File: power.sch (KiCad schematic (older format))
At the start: 25 parts, among them P24 CONN_2, Q1 MOS_P, Q2 MOS_N, Q3 MOS_P, SW3 SPST, SW4 SPST, U8 MCP73832, U9 MCP1700

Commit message: WT12 breakout headers are now in place
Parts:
- C17, C18, C19, C20: footprint (none) -> Capacitors_SMD:C_0805_HandSoldering
- JP3: footprint (none) -> replacement_kinesis_controller:JUMPER_3
- R11, R12, R13, R14, R15, R16, R17, R18, R19: footprint (none) -> Resistors_SMD:R_0805_HandSoldering
- SW3, SW4: footprint (none) -> replacement_kinesis_controller:Pin_Header_Staggered_Straight_1x02
- U9: footprint (none) -> Housings_SOT-23_SOT-143_TSOT-6:SOT23_Transistor_Handsoldering_RevB_14Mar2014
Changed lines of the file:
@@
 F 0 "C17" H 1100 1650 40  0000 L CNN
 F 1 "4.7uF" H 1100 1450 40  0000 L CNN
-F 2 "" H 1150 1400 30  0000 C CNN
+F 2 "Capacitors_SMD:C_0805_HandSoldering" H 1150 1400 30  0001 C CNN
 F 3 "" H 1050 1550 300 0000 C CNN
 	1    1050 1550
@@
 F 0 "D16" H 1500 1650 50  0000 C CNN
 F 1 "LED" H 1500 1450 50  0000 C CNN
-F 2 "" H 1500 1550 60  0000 C CNN
+F 2 "" H 1500 1550 60  0001 C CNN
 F 3 "" H 1500 1550 60  0000 C CNN
 	1    1500 1550
@@
 F 0 "U8" H 2900 1700 60  0000 C CNN
 F 1 "MCP73832" H 2900 1200 60  0000 C CNN
-F 2 "" H 2900 1500 60  0000 C CNN
+F 2 "" H 2900 1500 60  0001 C CNN
 F 3 "" H 2900 1500 60  0000 C CNN
 	1    2900 1500
@@
 F 0 "JP3" H 4200 1800 40  0000 L CNN
 F 1 "JUMPER3" H 4150 2000 40  0000 C CNN
-F 2 "" H 4150 1900 60  0000 C CNN
+F 2 "replacement_kinesis_controller:JUMPER_3" H 4150 1900 60  0001 C CNN
 F 3 "" H 4150 1900 60  0000 C CNN
 	1    4150 1900
@@
 F 0 "R18" V 3930 2200 40  0000 C CNN
 F 1 "2k" V 3857 2201 40  0000 C CNN
-F 2 "" V 3780 2200 30  0000 C CNN
+F 2 "Resistors_SMD:R_0805_HandSoldering" V 3780 2200 30  0001 C CNN
 F 3 "" H 3850 2200 30  0000 C CNN
 	1    3850 2200
@@
 F 0 "R19" V 4530 2200 40  0000 C CNN
 F 1 "10k" V 4457 2201 40  0000 C CNN
-F 2 "" V 4380 2200 30  0000 C CNN
+F 2 "Resistors_SMD:R_0805_HandSoldering" V 4380 2200 30  0001 C CNN
 F 3 "" H 4450 2200 30  0000 C CNN
 	1    4450 2200
@@
 F 0 "R20" V 4730 2200 40  0000 C CNN
 F 1 "EXTERNAL" V 4657 2201 40  0000 C CNN
-F 2 "" V 4580 2200 30  0000 C CNN
+F 2 "" V 4580 2200 30  0001 C CNN
 F 3 "" H 4650 2200 30  0000 C CNN
 	1    4650 2200
@@
 F 0 "C19" H 4900 1750 40  0000 L CNN
 F 1 "4.7uF" H 4900 1550 40  0000 L CNN
-F 2 "" H 4950 1500 30  0000 C CNN
+F 2 "Capacitors_SMD:C_0805_HandSoldering" H 4950 1500 30  0001 C CNN
 F 3 "" H 4850 1650 300 0000 C CNN
 	1    4850 1650
@@
 F 0 "R12" V 1930 1750 40  0000 C CNN
 F 1 "R" V 1857 1751 40  0000 C CNN
-F 2 "" V 1780 1750 30  0000 C CNN
+F 2 "Resistors_SMD:R_0805_HandSoldering" V 1780 1750 30  0001 C CNN
 F 3 "" H 1850 1750 30  0000 C CNN
 	1    1850 1750
@@
 F 0 "P24" V 5550 1550 40  0000 C CNN
 F 1 "CONN_2" V 5650 1550 40  0000 C CNN
-F 2 "" H 5600 1550 60  0000 C CNN
+F 2 "" H 5600 1550 60  0001 C CNN
 F 3 "" H 5600 1550 60  0000 C CNN
 	1    5600 1550
@@
 F 0 "Q3" H 3100 5890 60  0000 R CNN
 F 1 "MOS_P" H 3100 5520 60  0000 R CNN
-F 2 "" H 3100 5700 60  0000 C CNN
+F 2 "" H 3100 5700 60  0001 C CNN
 F 3 "" H 3100 5700 60  0000 C CNN
 	1    3100 5700
@@
 F 0 "Q2" H 2610 6070 60  0000 R CNN
 F 1 "MOS_N" H 2610 5750 60  0000 R CNN
-F 2 "" H 2600 5900 60  0000 C CNN
+F 2 "" H 2600 5900 60  0001 C CNN
 F 3 "" H 2600 5900 60  0000 C CNN
 	1    2600 5900
@@
 F 0 "R15" V 2780 5450 40  0000 C CNN
 F 1 "100k" V 2707 5451 40  0000 C CNN
-F 2 "" V 2630 5450 30  0000 C CNN
+F 2 "Resistors_SMD:R_0805_HandSoldering" V 2630 5450 30  0001 C CNN
 F 3 "" H 2700 5450 30  0000 C CNN
 	1    2700 5450
@@
 F 0 "R16" V 3280 6150 40  0000 C CNN
 F 1 "10k" V 3207 6151 40  0000 C CNN
-F 2 "" V 3130 6150 30  0000 C CNN
+F 2 "Resistors_SMD:R_0805_HandSoldering" V 3130 6150 30  0001 C CNN
 F 3 "" H 3200 6150 30  0000 C CNN
 	1    3200 6150
@@
 F 0 "R17" V 3280 6650 40  0000 C CNN
 F 1 "10k" V 3207 6651 40  0000 C CNN
-F 2 "" V 3130 6650 30  0000 C CNN
+F 2 "Resistors_SMD:R_0805_HandSoldering" V 3130 6650 30  0001 C CNN
 F 3 "" H 3200 6650 30  0000 C CNN
 	1    3200 6650
@@
 F 0 "Q1" H 2600 4090 60  0000 R CNN
 F 1 "MOS_P" H 2600 3720 60  0000 R CNN
-F 2 "" H 2600 3900 60  0000 C CNN
+F 2 "" H 2600 3900 60  0001 C CNN
 F 3 "" H 2600 3900 60  0000 C CNN
 	1    2600 3900
@@
 F 0 "C18" H 3250 4400 40  0000 L CNN
 F 1 "4.7uF" H 3250 4200 40  0000 L CNN
-F 2 "" H 3300 4150 30  0000 C CNN
+F 2 "Capacitors_SMD:C_0805_HandSoldering" H 3300 4150 30  0001 C CNN
 F 3 "" H 3200 4300 300 0000 C CNN
 	1    3200 4300
@@
 F 0 "D17" H 3000 3050 40  0000 C CNN
 F 1 "DIODESCH" H 3000 2850 40  0000 C CNN
-F 2 "" H 3000 2950 60  0000 C CNN
+F 2 "" H 3000 2950 60  0001 C CNN
 F 3 "" H 3000 2950 60  0000 C CNN
 	1    3000 2950
@@
 F 0 "U9" H 5400 3854 60  0000 C CNN
 F 1 "MCP1700" H 5250 4250 60  0000 C CNN
-F 2 "" H 5250 4050 60  0000 C CNN
+F 2 "Housings_SOT-23_SOT-143_TSOT-6:SOT23_Transistor_Handsoldering_RevB_14Mar2014" H 5250 4050 60  0001 C CNN
 F 3 "" H 5250 4050 60  0000 C CNN
 	1    5250 4050
@@
 F 0 "R11" V 880 4050 40  0000 C CNN
 F 1 "10k" V 807 4051 40  0000 C CNN
-F 2 "" V 730 4050 30  0000 C CNN
+F 2 "Resistors_SMD:R_0805_HandSoldering" V 730 4050 30  0001 C CNN
 F 3 "" H 800 4050 30  0000 C CNN
 	1    800  4050
@@
 F 0 "C20" H 6000 4400 40  0000 L CNN
 F 1 "4.7uF" H 6000 4200 40  0000 L CNN
-F 2 "" H 6050 4150 30  0000 C CNN
+F 2 "Capacitors_SMD:C_0805_HandSoldering" H 6050 4150 30  0001 C CNN
 F 3 "" H 5950 4300 300 0000 C CNN
 	1    5950 4300
@@
 F 0 "SW3" H 1700 4100 70  0000 C CNN
 F 1 "SPST" H 1700 3900 70  0000 C CNN
-F 2 "" H 1700 4000 60  0000 C CNN
+F 2 "replacement_kinesis_controller:Pin_Header_Staggered_Straight_1x02" H 1700 4000 60  0001 C CNN
 F 3 "" H 1700 4000 60  0000 C CNN
 	1    1700 4000
@@
 F 0 "R14" V 2680 3400 40  0000 C CNN
 F 1 "1k" V 2607 3401 40  0000 C CNN
-F 2 "" V 2530 3400 30  0000 C CNN
+F 2 "Resistors_SMD:R_0805_HandSoldering" V 2530 3400 30  0001 C CNN
 F 3 "" H 2600 3400 30  0000 C CNN
 	1    2600 3400
@@
 F 0 "R13" V 2330 6500 40  0000 C CNN
 F 1 "10k" V 2257 6501 40  0000 C CNN
-F 2 "" V 2180 6500 30  0000 C CNN
+F 2 "Resistors_SMD:R_0805_HandSoldering" V 2180 6500 30  0001 C CNN
 F 3 "" H 2250 6500 30  0000 C CNN
 	1    2250 6500
@@
 F 0 "SW4" H 4000 4100 70  0000 C CNN
 F 1 "SPST" H 4000 3900 70  0000 C CNN
-F 2 "" H 4000 4000 60  0000 C CNN
+F 2 "replacement_kinesis_controller:Pin_Header_Staggered_Straight_1x02" H 4000 4000 60  0001 C CNN
 F 3 "" H 4000 4000 60  0000 C CNN
 	1    4000 4000

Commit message: Add regular LED footprints
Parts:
- D16: footprint (none) -> LEDs:LED-0805
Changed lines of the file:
@@
 F 0 "D16" H 1500 1650 50  0000 C CNN
 F 1 "LED" H 1500 1450 50  0000 C CNN
-F 2 "" H 1500 1550 60  0001 C CNN
+F 2 "LEDs:LED-0805" H 1500 1550 60  0001 C CNN
 F 3 "" H 1500 1550 60  0000 C CNN
 	1    1500 1550

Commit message: More footprints
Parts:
- D17: footprint (none) -> replacement_kinesis_controller:SOD-123_Handsolder
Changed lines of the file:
@@
 F 0 "D17" H 3000 3050 40  0000 C CNN
 F 1 "DIODESCH" H 3000 2850 40  0000 C CNN
-F 2 "" H 3000 2950 60  0001 C CNN
+F 2 "replacement_kinesis_controller:SOD-123_Handsolder" H 3000 2950 60  0001 C CNN
 F 3 "" H 3000 2950 60  0000 C CNN
 	1    3000 2950

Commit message: Add more footprint mappings
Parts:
- Q1: footprint (none) -> SMD_Packages:DPAK-2-1EP_GDS
- Q2, Q3: footprint (none) -> Housings_SOT-23_SOT-143_TSOT-6:SOT23_Handsoldering
- U8: footprint (none) -> Housings_SOT-23_SOT-143_TSOT-6:SOT23-5
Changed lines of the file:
@@
 F 0 "U8" H 2900 1700 60  0000 C CNN
 F 1 "MCP73832" H 2900 1200 60  0000 C CNN
-F 2 "" H 2900 1500 60  0001 C CNN
+F 2 "Housings_SOT-23_SOT-143_TSOT-6:SOT23-5" H 2900 1500 60  0001 C CNN
 F 3 "" H 2900 1500 60  0000 C CNN
 	1    2900 1500
@@
 F 0 "Q3" H 3100 5890 60  0000 R CNN
 F 1 "MOS_P" H 3100 5520 60  0000 R CNN
-F 2 "" H 3100 5700 60  0001 C CNN
+F 2 "Housings_SOT-23_SOT-143_TSOT-6:SOT23_Handsoldering" H 3100 5700 60  0001 C CNN
 F 3 "" H 3100 5700 60  0000 C CNN
 	1    3100 5700
@@
 F 0 "Q2" H 2610 6070 60  0000 R CNN
 F 1 "MOS_N" H 2610 5750 60  0000 R CNN
-F 2 "" H 2600 5900 60  0001 C CNN
+F 2 "Housings_SOT-23_SOT-143_TSOT-6:SOT23_Handsoldering" H 2600 5900 60  0001 C CNN
 F 3 "" H 2600 5900 60  0000 C CNN
 	1    2600 5900
@@
 F 0 "Q1" H 2600 4090 60  0000 R CNN
 F 1 "MOS_P" H 2600 3720 60  0000 R CNN
-F 2 "" H 2600 3900 60  0001 C CNN
+F 2 "SMD_Packages:DPAK-2-1EP_GDS" H 2600 3900 60  0001 C CNN
 F 3 "" H 2600 3900 60  0000 C CNN
 	1    2600 3900

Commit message: Basically done footprint assignment now...?
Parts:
- P24: footprint (none) -> replacement_kinesis_controller:JST-2
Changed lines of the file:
@@
 F 0 "P24" V 5550 1550 40  0000 C CNN
 F 1 "CONN_2" V 5650 1550 40  0000 C CNN
-F 2 "" H 5600 1550 60  0001 C CNN
+F 2 "replacement_kinesis_controller:JST-2" H 5600 1550 60  0001 C CNN
 F 3 "" H 5600 1550 60  0000 C CNN
 	1    5600 1550

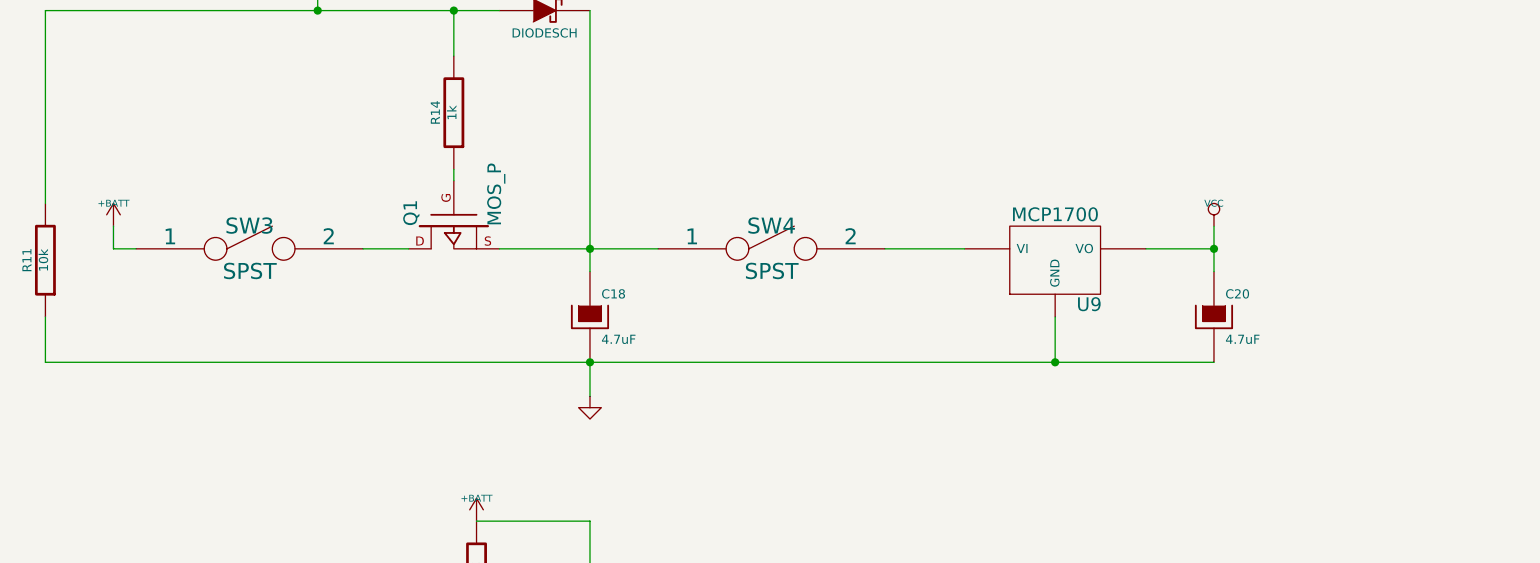
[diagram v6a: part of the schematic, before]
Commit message: A bunch of footprint arranging
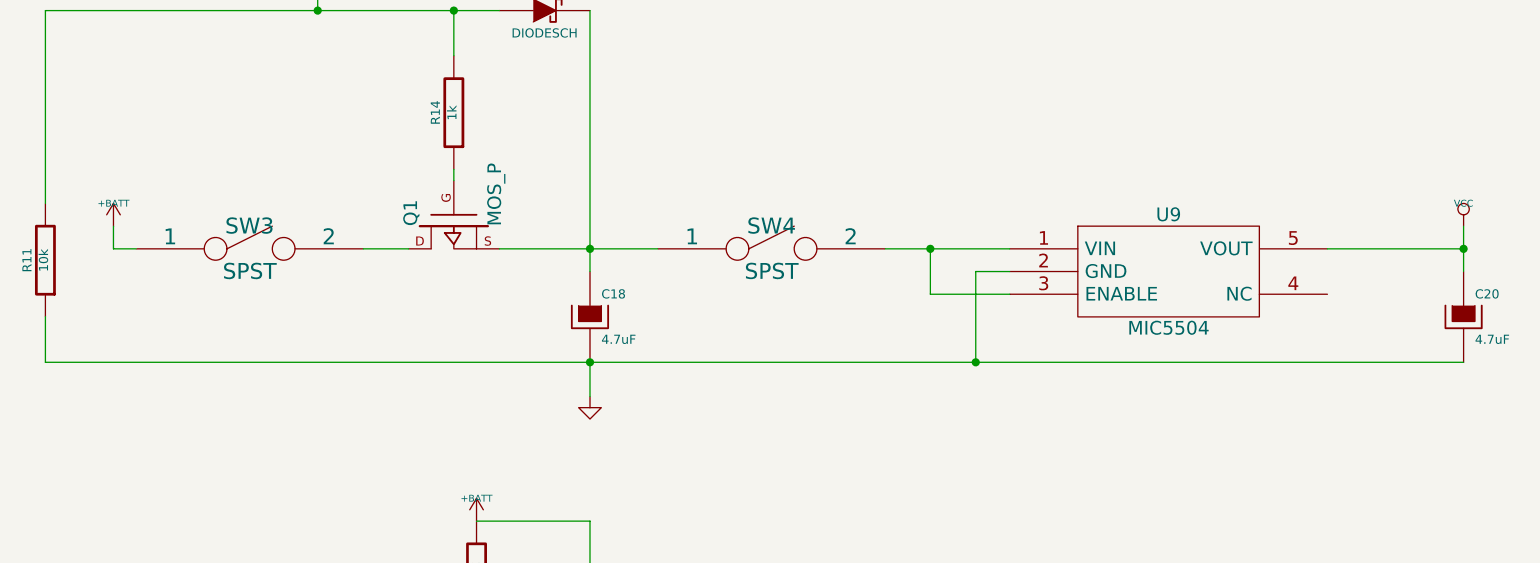
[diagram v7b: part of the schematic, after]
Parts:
- removed U9: MCP1700, Housings_SOT-23_SOT-143_TSOT-6:SOT23_Transistor_Handsoldering_RevB_14Mar2014, symbol MCP1700
- added U9: MIC5504, Housings_SOT-23_SOT-143_TSOT-6:SOT23-5, symbol MIC5504
- Q1: footprint SMD_Packages:DPAK-2-1EP_GDS -> replacement_kinesis_controller:SOT23_Handsoldering
- Q2, Q3: footprint Housings_SOT-23_SOT-143_TSOT-6:SOT23_Handsoldering -> replacement_kinesis_controller:SOT23_Handsoldering
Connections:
- net GND: now also U9.2 (GND)
- net VCC: now also U9.5 (VOUT)
- net at SW4.2: now also U9.1 (VIN), U9.3 (ENABLE)
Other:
- moved on the sheet: C20
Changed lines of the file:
@@
 $EndDescr
 $Comp
-L +5V #PWR56
+L +5V #PWR056
 U 1 1 54E62CDB
 P 1050 1250
-F 0 "#PWR56" H 1050 1340 20  0001 C CNN
+F 0 "#PWR056" H 1050 1340 20  0001 C CNN
 F 1 "+5V" H 1050 1340 30  0000 C CNN
 F 2 "" H 1050 1250 60  0000 C CNN
@@
 $EndComp
 $Comp
-L GND #PWR57
+L GND #PWR057
 U 1 1 54E62CE1
 P 1050 1850
-F 0 "#PWR57" H 1050 1850 30  0001 C CNN
+F 0 "#PWR057" H 1050 1850 30  0001 C CNN
 F 1 "GND" H 1050 1780 30  0001 C CNN
 F 2 "" H 1050 1850 60  0000 C CNN
@@
 $EndComp
 $Comp
-L GND #PWR63
+L GND #PWR058
 U 1 1 54E62D26
 P 3600 2550
-F 0 "#PWR63" H 3600 2550 30  0001 C CNN
+F 0 "#PWR058" H 3600 2550 30  0001 C CNN
 F 1 "GND" H 3600 2480 30  0001 C CNN
 F 2 "" H 3600 2550 60  0000 C CNN
@@
 $EndComp
 $Comp
-L GND #PWR64
+L GND #PWR059
 U 1 1 54E62D2C
 P 3850 2550
-F 0 "#PWR64" H 3850 2550 30  0001 C CNN
+F 0 "#PWR059" H 3850 2550 30  0001 C CNN
 F 1 "GND" H 3850 2480 30  0001 C CNN
 F 2 "" H 3850 2550 60  0000 C CNN
@@
 $EndComp
 $Comp
-L GND #PWR65
+L GND #PWR060
 U 1 1 54E62D32
 P 4450 2550
-F 0 "#PWR65" H 4450 2550 30  0001 C CNN
+F 0 "#PWR060" H 4450 2550 30  0001 C CNN
 F 1 "GND" H 4450 2480 30  0001 C CNN
 F 2 "" H 4450 2550 60  0000 C CNN
@@
 $EndComp
 $Comp
-L GND #PWR66
+L GND #PWR061
 U 1 1 54E62D38
 P 4650 2550
-F 0 "#PWR66" H 4650 2550 30  0001 C CNN
+F 0 "#PWR061" H 4650 2550 30  0001 C CNN
 F 1 "GND" H 4650 2480 30  0001 C CNN
 F 2 "" H 4650 2550 60  0000 C CNN
@@
 $EndComp
 $Comp
-L GND #PWR68
+L GND #PWR062
 U 1 1 54E62D3E
 P 4850 2550
-F 0 "#PWR68" H 4850 2550 30  0001 C CNN
+F 0 "#PWR062" H 4850 2550 30  0001 C CNN
 F 1 "GND" H 4850 2480 30  0001 C CNN
 F 2 "" H 4850 2550 60  0000 C CNN
@@
 $EndComp
 $Comp
-L +BATT #PWR67
+L +BATT #PWR063
 U 1 1 54E62D44
 P 4850 1350
-F 0 "#PWR67" H 4850 1300 20  0001 C CNN
+F 0 "#PWR063" H 4850 1300 20  0001 C CNN
 F 1 "+BATT" H 4850 1450 30  0000 C CNN
 F 2 "" H 4850 1350 60  0000 C CNN
@@
 $EndComp
 $Comp
-L GND #PWR69
+L GND #PWR064
 U 1 1 54E62D51
 P 5250 2550
-F 0 "#PWR69" H 5250 2550 30  0001 C CNN
+F 0 "#PWR064" H 5250 2550 30  0001 C CNN
 F 1 "GND" H 5250 2480 30  0001 C CNN
 F 2 "" H 5250 2550 60  0000 C CNN
@@
 F 0 "Q3" H 3100 5890 60  0000 R CNN
 F 1 "MOS_P" H 3100 5520 60  0000 R CNN
-F 2 "Housings_SOT-23_SOT-143_TSOT-6:SOT23_Handsoldering" H 3100 5700 60  0001 C CNN
+F 2 "replacement_kinesis_controller:SOT23_Handsoldering" H 3100 5700 60  0001 C CNN
 F 3 "" H 3100 5700 60  0000 C CNN
 	1    3100 5700
@@
 F 0 "Q2" H 2610 6070 60  0000 R CNN
 F 1 "MOS_N" H 2610 5750 60  0000 R CNN
-F 2 "Housings_SOT-23_SOT-143_TSOT-6:SOT23_Handsoldering" H 2600 5900 60  0001 C CNN
+F 2 "replacement_kinesis_controller:SOT23_Handsoldering" H 2600 5900 60  0001 C CNN
 F 3 "" H 2600 5900 60  0000 C CNN
 	1    2600 5900
@@
 	3200 6400 3500 6400
 $Comp
-L +BATT #PWR60
+L +BATT #PWR065
 U 1 1 54E64283
 P 2700 5200
-F 0 "#PWR60" H 2700 5150 20  0001 C CNN
+F 0 "#PWR065" H 2700 5150 20  0001 C CNN
 F 1 "+BATT" H 2700 5300 30  0000 C CNN
 F 2 "" H 2700 5200 60  0000 C CNN
@@
 $EndComp
 $Comp
-L GND #PWR62
+L GND #PWR066
 U 1 1 54E64289
 P 3200 7000
-F 0 "#PWR62" H 3200 7000 30  0001 C CNN
+F 0 "#PWR066" H 3200 7000 30  0001 C CNN
 F 1 "GND" H 3200 6930 30  0001 C CNN
 F 2 "" H 3200 7000 60  0000 C CNN
@@
 F 0 "Q1" H 2600 4090 60  0000 R CNN
 F 1 "MOS_P" H 2600 3720 60  0000 R CNN
-F 2 "SMD_Packages:DPAK-2-1EP_GDS" H 2600 3900 60  0001 C CNN
+F 2 "replacement_kinesis_controller:SOT23_Handsoldering" H 2600 3900 60  0001 C CNN
 F 3 "" H 2600 3900 60  0000 C CNN
 	1    2600 3900
@@
 $EndComp
 $Comp
-L +BATT #PWR58
+L +BATT #PWR067
 U 1 1 54E64297
 P 1100 3900
-F 0 "#PWR58" H 1100 3850 20  0001 C CNN
+F 0 "#PWR067" H 1100 3850 20  0001 C CNN
 F 1 "+BATT" H 1100 4000 30  0000 C CNN
 F 2 "" H 1100 3900 60  0000 C CNN
@@
 $EndComp
 $Comp
-L MCP1700 U9
-U 1 1 54E642AB
-P 5250 4050
-F 0 "U9" H 5400 3854 60  0000 C CNN
-F 1 "MCP1700" H 5250 4250 60  0000 C CNN
-F 2 "Housings_SOT-23_SOT-143_TSOT-6:SOT23_Transistor_Handsoldering_RevB_14Mar2014" H 5250 4050 60  0001 C CNN
-F 3 "" H 5250 4050 60  0000 C CNN
-	1    5250 4050
-	1    0    0    -1
-$EndComp
-$Comp
-L VCC #PWR70
+L VCC #PWR068
 U 1 1 54E642B2
-P 5950 3900
-F 0 "#PWR70" H 5950 4000 30  0001 C CNN
-F 1 "VCC" H 5950 4000 30  0000 C CNN
-F 2 "" H 5950 3900 60  0000 C CNN
-F 3 "" H 5950 3900 60  0000 C CNN
-	1    5950 3900
+P 7050 3900
+F 0 "#PWR068" H 7050 4000 30  0001 C CNN
+F 1 "VCC" H 7050 4000 30  0000 C CNN
+F 2 "" H 7050 3900 60  0000 C CNN
+F 3 "" H 7050 3900 60  0000 C CNN
+	1    7050 3900
 	1    0    0    -1
 $EndComp
@@
 	800  2950 2800 2950
 $Comp
-L +5V #PWR59
+L +5V #PWR069
 U 1 1 54E642BF
 P 2000 2850
-F 0 "#PWR59" H 2000 2940 20  0001 C CNN
+F 0 "#PWR069" H 2000 2940 20  0001 C CNN
 F 1 "+5V" H 2000 2940 30  0000 C CNN
 F 2 "" H 2000 2850 60  0000 C CNN
@@
 Connection ~ 2600 2950
 Wire Wire Line
-	5650 4000 5950 4000
-Wire Wire Line
-	5950 3900 5950 4100
-$Comp
-L GND #PWR61
+	6450 4000 7050 4000
+Wire Wire Line
+	7050 3900 7050 4100
+$Comp
+L GND #PWR070
 U 1 1 54E642C9
 P 3200 4650
-F 0 "#PWR61" H 3200 4650 30  0001 C CNN
+F 0 "#PWR070" H 3200 4650 30  0001 C CNN
 F 1 "GND" H 3200 4580 30  0001 C CNN
 F 2 "" H 3200 4650 60  0000 C CNN
@@
 $EndComp
 Wire Wire Line
-	800  4500 5950 4500
+	800  4500 7050 4500
 $Comp
 L R R11
@@
 L CP C20
 U 1 1 54E642DD
-P 5950 4300
-F 0 "C20" H 6000 4400 40  0000 L CNN
-F 1 "4.7uF" H 6000 4200 40  0000 L CNN
-F 2 "Capacitors_SMD:C_0805_HandSoldering" H 6050 4150 30  0001 C CNN
-F 3 "" H 5950 4300 300 0000 C CNN
-	1    5950 4300
-	1    0    0    -1
-$EndComp
-Connection ~ 5950 4000
+P 7050 4300
+F 0 "C20" H 7100 4400 40  0000 L CNN
+F 1 "4.7uF" H 7100 4200 40  0000 L CNN
+F 2 "Capacitors_SMD:C_0805_HandSoldering" H 7150 4150 30  0001 C CNN
+F 3 "" H 7050 4300 300 0000 C CNN
+	1    7050 4300
+	1    0    0    -1
+$EndComp
+Connection ~ 7050 4000
 $Comp
 L SPST SW3
@@
 $EndComp
 Wire Wire Line
-	4500 4000 4850 4000
-Wire Wire Line
-	5250 4300 5250 4500
-Connection ~ 5250 4500
+	4500 4000 5050 4000
 Wire Wire Line
 	3200 4500 3200 4650
+$Comp
+L MIC5504 U9
+U 1 1 54EBFAD3
+P 5750 4050
+F 0 "U9" H 5750 4250 60  0000 C CNN
+F 1 "MIC5504" H 5750 3750 60  0000 C CNN
+F 2 "Housings_SOT-23_SOT-143_TSOT-6:SOT23-5" H 5750 4050 60  0001 C CNN
+F 3 "" H 5750 4050 60  0000 C CNN
+	1    5750 4050
+	1    0    0    -1
+$EndComp
+Wire Wire Line
+	5050 4200 4700 4200
+Wire Wire Line
+	4700 4200 4700 4000
+Connection ~ 4700 4000
+Wire Wire Line
+	5050 4100 4900 4100
+Wire Wire Line
+	4900 4100 4900 4500
+Connection ~ 4900 4500
 $EndSCHEMATC
